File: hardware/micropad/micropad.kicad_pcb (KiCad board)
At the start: 2 copper layers, 45.1 x 76.5 mm, 32 parts, among them J1 SWD Debug, J3 USB_B_Micro, SW1 SW_SPST, SW2 SW_SPST, SW3 SW_SPST, U1 LD1117S33TR_SOT223, U2 STM32F042K6Ux, U3 APA102

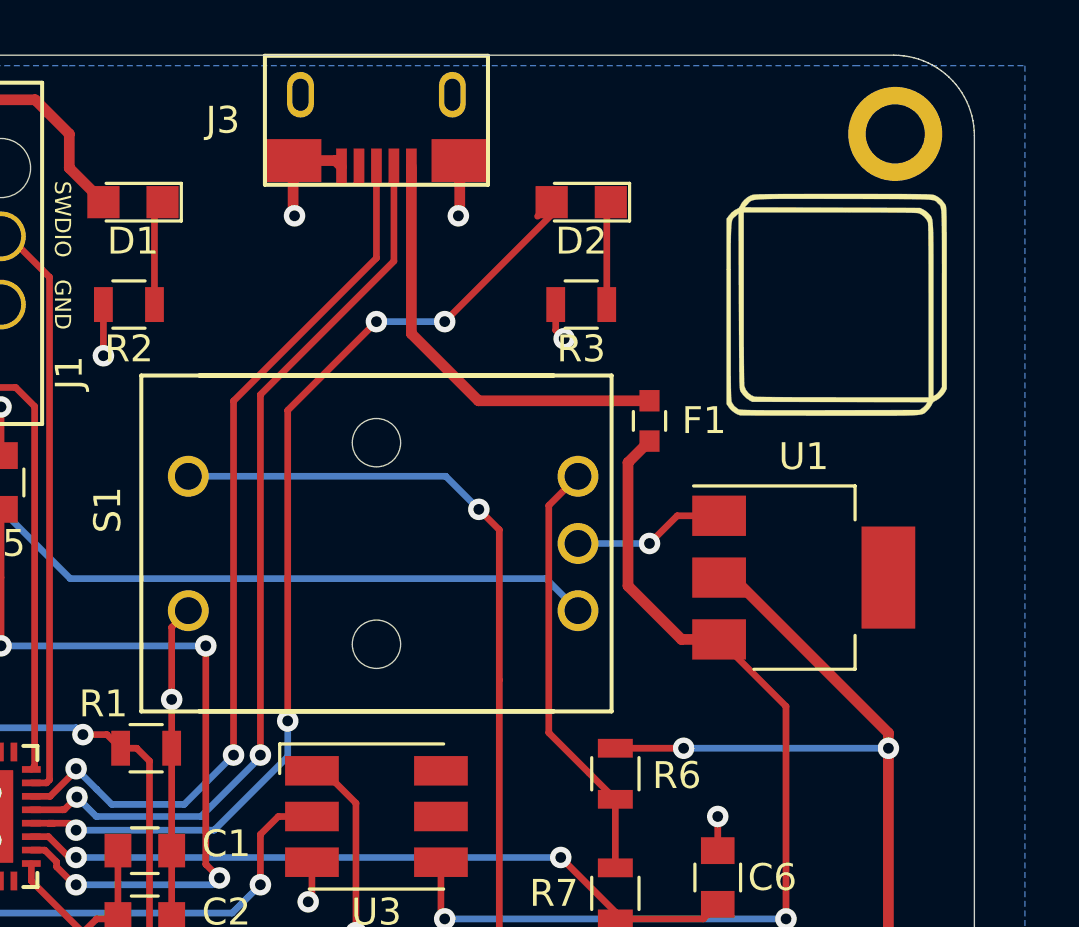
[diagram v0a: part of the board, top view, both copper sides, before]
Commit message: Replace USB micro connector with USB-C connector
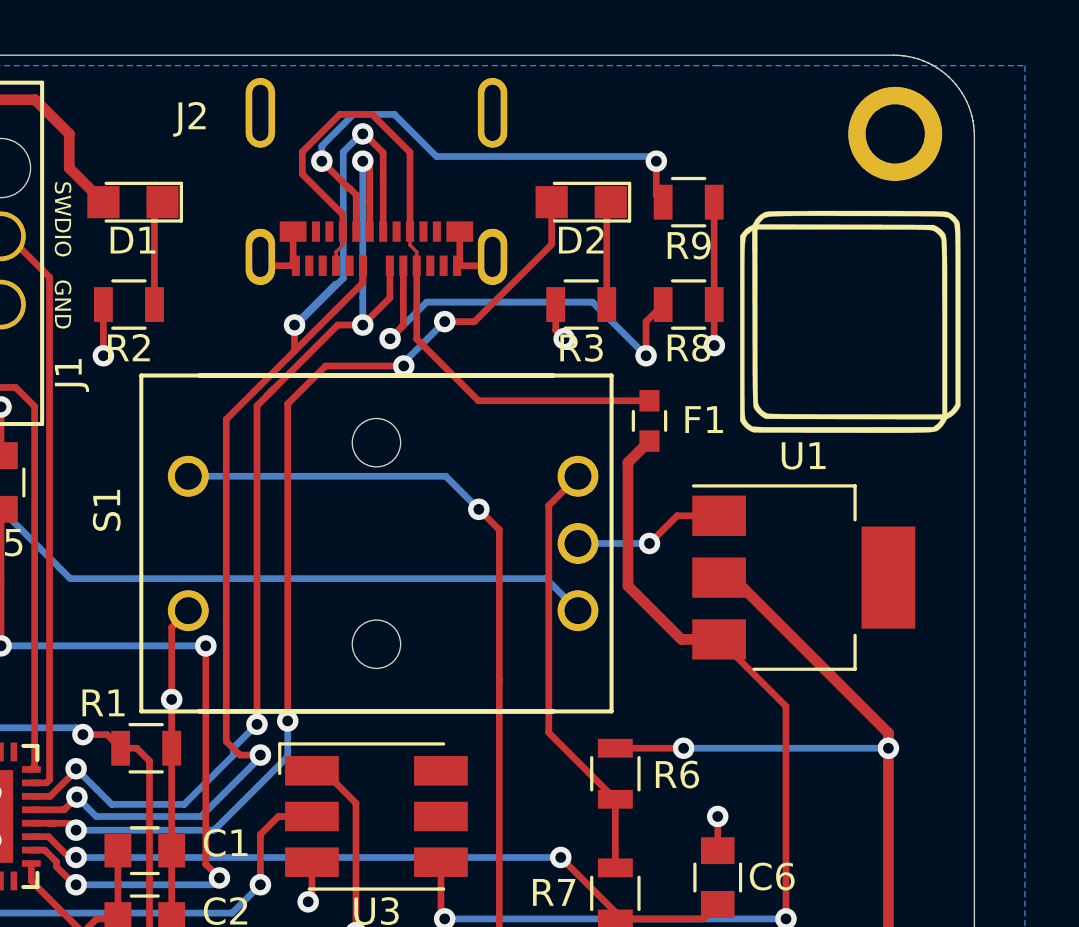
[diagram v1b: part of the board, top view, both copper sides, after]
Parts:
- removed J3: USB_B_Micro, micropad:XKB-U254_USB
- added J2: USB_C_Receptacle_USB2.0, micropad:USB_C_Receptacle_Molex_1054500101, F.Cu at (53.3, 27.3)
- added R8: 5.1k, Resistors_SMD:R_0805, F.Cu at (65.0, 31.8)
- added R9: 5.1k, Resistors_SMD:R_0805, F.Cu at (65.0, 27.9)
- moved G*** 0.81 mm to (71.0, 32.4)
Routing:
- net Net-(J2-PadB5): track 0.00 -> 19.0 mm, vias 0 -> 2
- net Net-(J2-PadA5): track 0.00 -> 16.0 mm, vias 0 -> 2
- net /USB_DM: track 34.0 -> 46.7 mm, vias 2 -> 4
- net Net-(F1-Pad2): track 16.1 -> 26.8 mm
- net /USB_DP: track 33.4 -> 39.9 mm, vias 2 -> 4
- net GND: track 49.0 -> 53.4 mm, vias 17 -> 16
- net /LED_USR: track 37.9 -> 38.5 mm

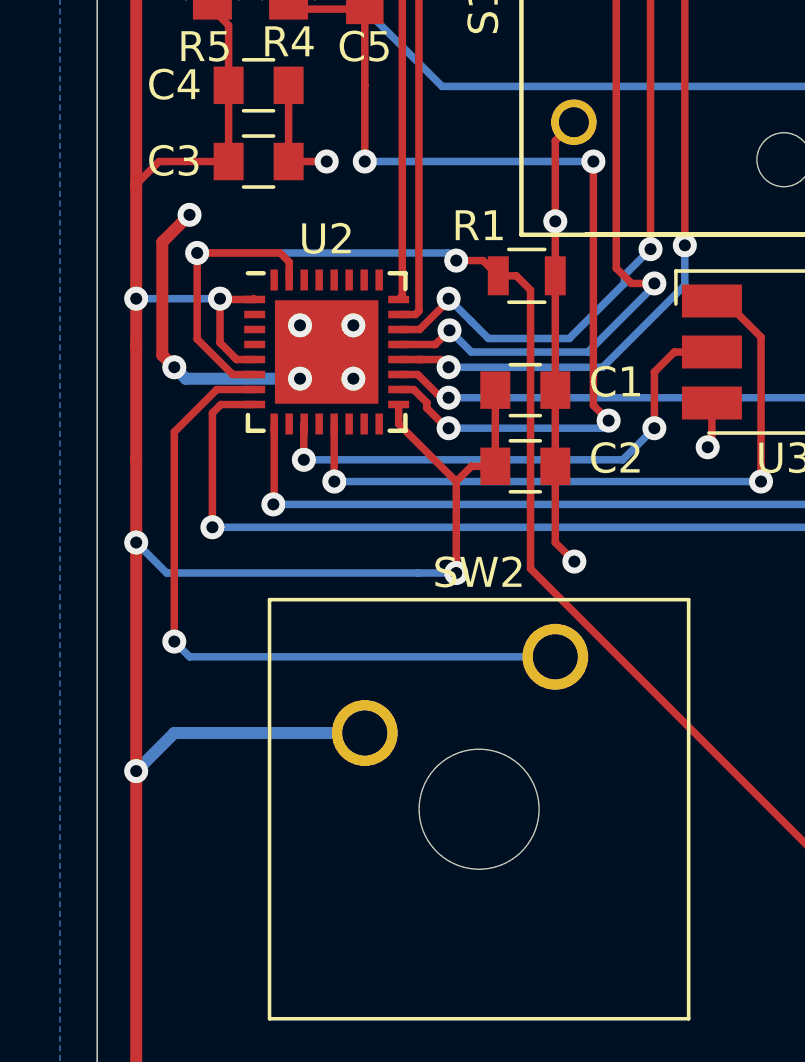
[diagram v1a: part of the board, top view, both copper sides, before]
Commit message: Add additional ground connections to the STM32
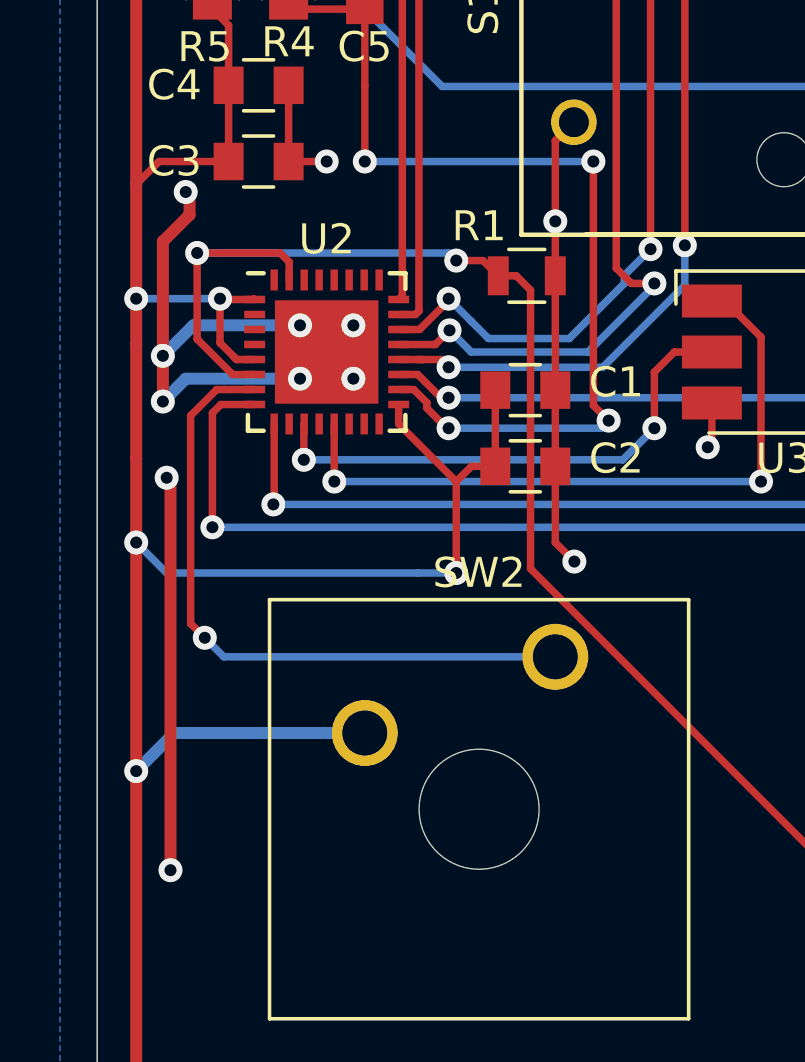
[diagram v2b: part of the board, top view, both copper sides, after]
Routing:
- net GND: track 53.4 -> 73.9 mm, vias 16 -> 19
- net Net-(SW2-Pad1): track 23.2 -> 22.0 mm
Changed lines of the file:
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@@
     (thickness 1.6)
     (drawings 421)
-    (tracks 359)
+    (tracks 371)
     (zones 0)
     (modules 34)
@@
   )
   (setup
-    (last_trace_width 0.25)
+    (last_trace_width 0.4)
     (user_trace_width 0.127)
     (user_trace_width 0.4)
@@
   (segment (start 45.72 46.445) (end 45.72 43.76) (width 0.25) (layer F.Cu) (net 2))
   (segment (start 63.5 40.64) (end 60.84 40.64) (width 0.25) (layer B.Cu) (net 2))
-  (via (at 33.02 51.308) (size 0.8) (drill 0.4) (layers F.Cu B.Cu) (net 2))
-  (segment (start 33.401 51.689) (end 33.02 51.308) (width 0.4) (layer B.Cu) (net 2))
   (segment (start 37.211 51.689) (end 33.401 51.689) (width 0.4) (layer B.Cu) (net 2))
-  (segment (start 32.620001 47.135999) (end 33.528 46.228) (width 0.4) (layer F.Cu) (net 2))
-  (via (at 33.528 46.228) (size 0.8) (drill 0.4) (layers F.Cu B.Cu) (net 2))
-  (segment (start 32.620001 50.908001) (end 32.620001 47.135999) (width 0.4) (layer F.Cu) (net 2))
-  (segment (start 33.02 51.308) (end 32.620001 50.908001) (width 0.4) (layer F.Cu) (net 2))
   (segment (start 49.35 30.305) (end 49.02 29.975) (width 0.25) (layer F.Cu) (net 2))
   (segment (start 50.34 30.305) (end 49.35 30.305) (width 0.25) (layer F.Cu) (net 2))
@@
   (segment (start 65.908 33.269) (end 65.913 33.274) (width 0.25) (layer F.Cu) (net 2))
   (segment (start 65.908 31.75) (end 65.908 33.269) (width 0.25) (layer F.Cu) (net 2))
+  (via (at 32.893 68.072) (size 0.8) (drill 0.4) (layers F.Cu B.Cu) (net 2))
+  (via (at 33.401 45.466) (size 0.8) (drill 0.4) (layers F.Cu B.Cu) (net 2))
+  (via (at 32.766 54.991) (size 0.8) (drill 0.4) (layers F.Cu B.Cu) (net 2))
+  (segment (start 32.893 55.118) (end 32.766 54.991) (width 0.4) (layer F.Cu) (net 2))
+  (segment (start 32.893 68.072) (end 32.893 55.118) (width 0.4) (layer F.Cu) (net 2))
+  (via (at 32.639 52.451) (size 0.8) (drill 0.4) (layers F.Cu B.Cu) (net 2))
+  (segment (start 33.401 51.689) (end 32.639 52.451) (width 0.4) (layer B.Cu) (net 2))
+  (segment (start 32.639 50.927) (end 32.620001 50.908001) (width 0.4) (layer F.Cu) (net 2))
+  (segment (start 32.639 52.451) (end 32.639 50.927) (width 0.4) (layer F.Cu) (net 2))
+  (segment (start 33.528 45.593) (end 33.401 45.466) (width 0.4) (layer F.Cu) (net 2))
+  (segment (start 33.528 46.228) (end 33.528 45.593) (width 0.4) (layer F.Cu) (net 2))
+  (segment (start 32.639 47.117) (end 33.528 46.228) (width 0.4) (layer F.Cu) (net 2))
+  (segment (start 32.639 50.927) (end 32.639 47.117) (width 0.4) (layer F.Cu) (net 2))
+  (via (at 32.639 50.927) (size 0.8) (drill 0.4) (layers F.Cu B.Cu) (net 2))
+  (segment (start 33.655 49.911) (end 32.639 50.927) (width 0.4) (layer B.Cu) (net 2))
+  (segment (start 37.211 49.911) (end 33.655 49.911) (width 0.4) (layer B.Cu) (net 2))
   (via (at 42.164 53.34) (size 0.8) (drill 0.4) (layers F.Cu B.Cu) (net 3))
   (segment (start 42.106998 53.34) (end 42.164 53.34) (width 0.25) (layer F.Cu) (net 3))
@@
   (segment (start 52.84 30.935) (end 51.7935 31.9815) (width 0.25) (layer F.Cu) (net 11))
   (segment (start 49.022 34.753) (end 48.768 35.007) (width 0.25) (layer F.Cu) (net 11))
-  (via (at 50.292 32.512) (size 0.8) (drill 0.4) (layers F.Cu B.Cu) (net 11))
-  (segment (start 50.292 32.512) (end 50.292 33.483) (width 0.25) (layer F.Cu) (net 11))
   (segment (start 50.2695 33.5055) (end 49.022 34.753) (width 0.25) (layer F.Cu) (net 11))
   (segment (start 50.292 33.483) (end 50.2695 33.5055) (width 0.25) (layer F.Cu) (net 11))
@@
   (segment (start 47.752 36.023) (end 48.768 35.007) (width 0.25) (layer F.Cu) (net 11))
   (segment (start 47.752 48.006) (end 47.752 36.023) (width 0.25) (layer F.Cu) (net 11))
+  (segment (start 50.292 32.512) (end 50.292 33.483) (width 0.25) (layer F.Cu) (net 11))
+  (via (at 50.292 32.512) (size 0.8) (drill 0.4) (layers F.Cu B.Cu) (net 11) (status 1000000))
   (segment (start 40.5 50.05) (end 41.196412 50.05) (width 0.25) (layer F.Cu) (net 12))
   (segment (start 46.186007 50.34999) (end 43.49199 50.34999) (width 0.25) (layer B.Cu) (net 12))
@@
   (segment (start 57.15 39.37) (end 57.912 40.132) (width 0.25) (layer F.Cu) (net 16))
   (segment (start 46.34 38.14) (end 55.92 38.14) (width 0.25) (layer B.Cu) (net 16))
-  (segment (start 33.528 60.96) (end 33.02 60.452) (width 0.25) (layer B.Cu) (net 17))
-  (via (at 33.02 60.452) (size 0.8) (drill 0.4) (layers F.Cu B.Cu) (net 17))
-  (segment (start 45.72 60.96) (end 33.528 60.96) (width 0.25) (layer B.Cu) (net 17))
-  (segment (start 34.43559 52.05) (end 35.7 52.05) (width 0.25) (layer F.Cu) (net 17))
-  (segment (start 33.02 53.46559) (end 34.43559 52.05) (width 0.25) (layer F.Cu) (net 17))
-  (segment (start 33.02 60.452) (end 33.02 53.46559) (width 0.25) (layer F.Cu) (net 17))
+  (via (at 34.036 60.325) (size 0.8) (drill 0.4) (layers F.Cu B.Cu) (net 17))
+  (segment (start 34.671 60.96) (end 34.036 60.325) (width 0.25) (layer B.Cu) (net 17))
+  (segment (start 45.72 60.96) (end 34.671 60.96) (width 0.25) (layer B.Cu) (net 17))
+  (segment (start 34.43559 52.05) (end 34.691 52.05) (width 0.25) (layer F.Cu) (net 17))
+  (segment (start 33.564999 52.920591) (end 34.43559 52.05) (width 0.25) (layer F.Cu) (net 17))
+  (segment (start 33.564999 59.853999) (end 33.564999 52.920591) (width 0.25) (layer F.Cu) (net 17))
+  (segment (start 34.036 60.325) (end 33.564999 59.853999) (width 0.25) (layer F.Cu) (net 17))
+  (segment (start 34.691 52.05) (end 35.7 52.05) (width 0.25) (layer F.Cu) (net 17))
   (segment (start 35.7 52.55) (end 34.572 52.55) (width 0.25) (layer F.Cu) (net 18))
   (via (at 34.29 56.642) (size 0.8) (drill 0.4) (layers F.Cu B.Cu) (net 18))

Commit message: Revision 2
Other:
- board text added: "micropad rev. 2"
- board text removed: "micropad rev. 1"
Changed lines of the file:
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@@
     )
   )
-  (gr_text "micropad rev. 1" (at 74.295 84.455 90) (layer F.SilkS)
+  (gr_text "micropad rev. 2" (at 74.295 84.455 90) (layer F.SilkS)
     (effects (font (size 1.5 1.5) (thickness 0.3)))
   )

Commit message: Change PCB mounting holes to M3
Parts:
- H1, H2, H3, H4: footprint Mounting_Holes:MountingHole_2.2mm_M2_ISO7380_Pad -> Mounting_Holes:MountingHole_3.2mm_M3_ISO7380_Pad
- moved J1 2.54 mm to (40.6, 29.8)
- moved H3 1.98 mm to (71.1, 26.7)
- moved R2 1.91 mm to (46.0, 31.8)
- moved G*** 1.91 mm to (71.1, 34.3)
- moved H1 1.80 mm to (34.3, 26.7)
- moved H4 1.70 mm to (71.1, 95.2)
- moved D1 1.61 mm to (45.9, 27.9)
- moved H2 1.48 mm to (34.3, 95.2)
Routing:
- net /SWCLK: track 26.0 -> 20.5 mm
- net GND: track 73.9 -> 78.5 mm, vias 19 -> 20
- net +3V3: track 241.1 -> 237.8 mm
- net /SWDIO: track 21.5 -> 22.8 mm

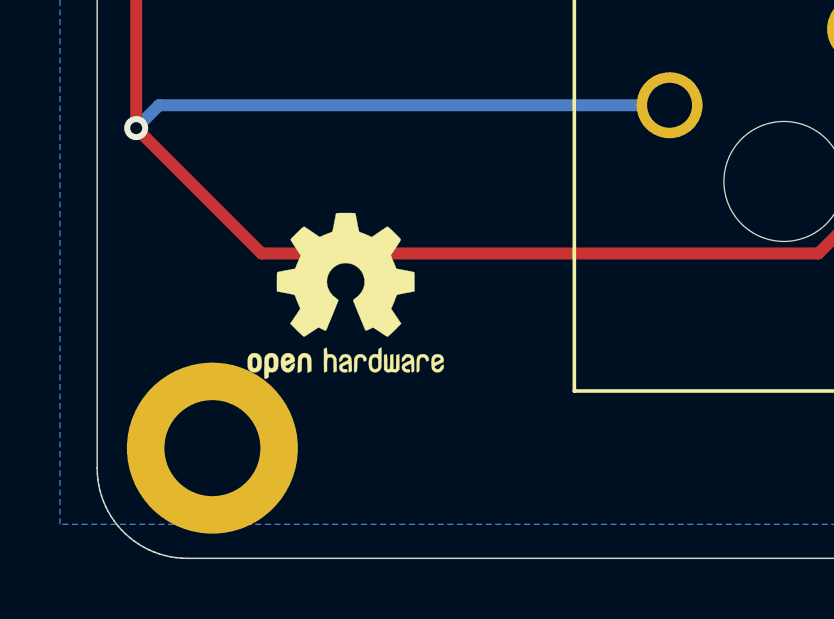
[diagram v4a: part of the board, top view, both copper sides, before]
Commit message: Order rev. 2 of PCB
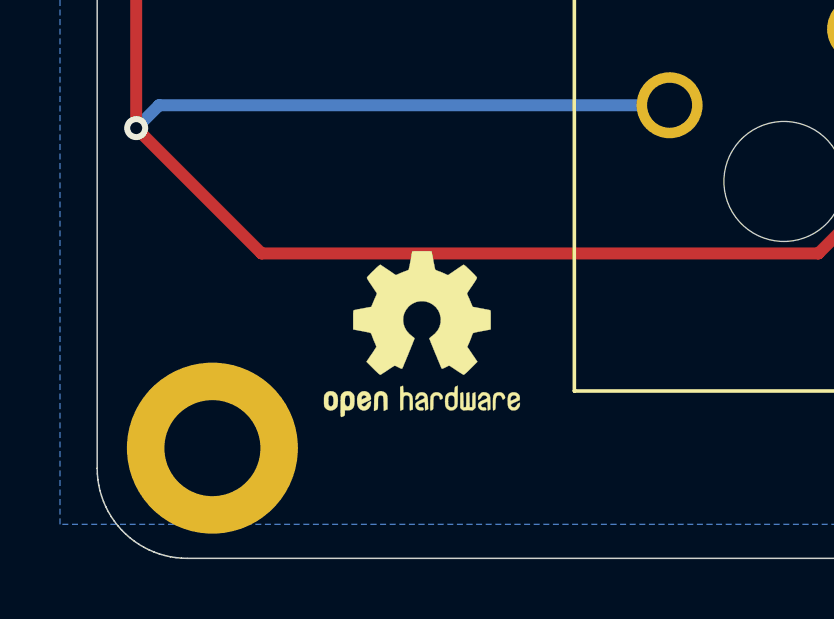
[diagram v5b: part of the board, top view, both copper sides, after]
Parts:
- moved REF*** 2.84 mm to (41.3, 91.4)
